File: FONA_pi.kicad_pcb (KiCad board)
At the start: 2 copper layers, 88.4 x 59.1 mm, 35 parts, among them J1 Conn_01x20_Socket, J10 Conn_01x04_Pin, J11 Conn_01x20_Socket, J12 Conn_01x20_Socket, J13 Conn_01x06_Socket, J14 Conn_01x06_Socket, J15 Conn_01x06_Socket, J16 Conn_01x06_Socket, J17 Conn_01x06_Socket, J18 Conn_01x04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

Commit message: Placed footprints again.
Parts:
- removed REF** (x4): MountingHole_2.1mm, MountingHole:MountingHole_2.1mm
- moved JP4 2.58 mm to (144.2, 96.9)
- moved JP3 1.62 mm to (144.2, 93.3)
- moved JP2 0.66 mm to (144.2, 89.8)
- moved J16 0.41 mm to (124.1, 78.4)
- moved JP1 0.27 mm to (144.2, 86.2)
- moved J17 0.18 mm to (124.9, 112.9)

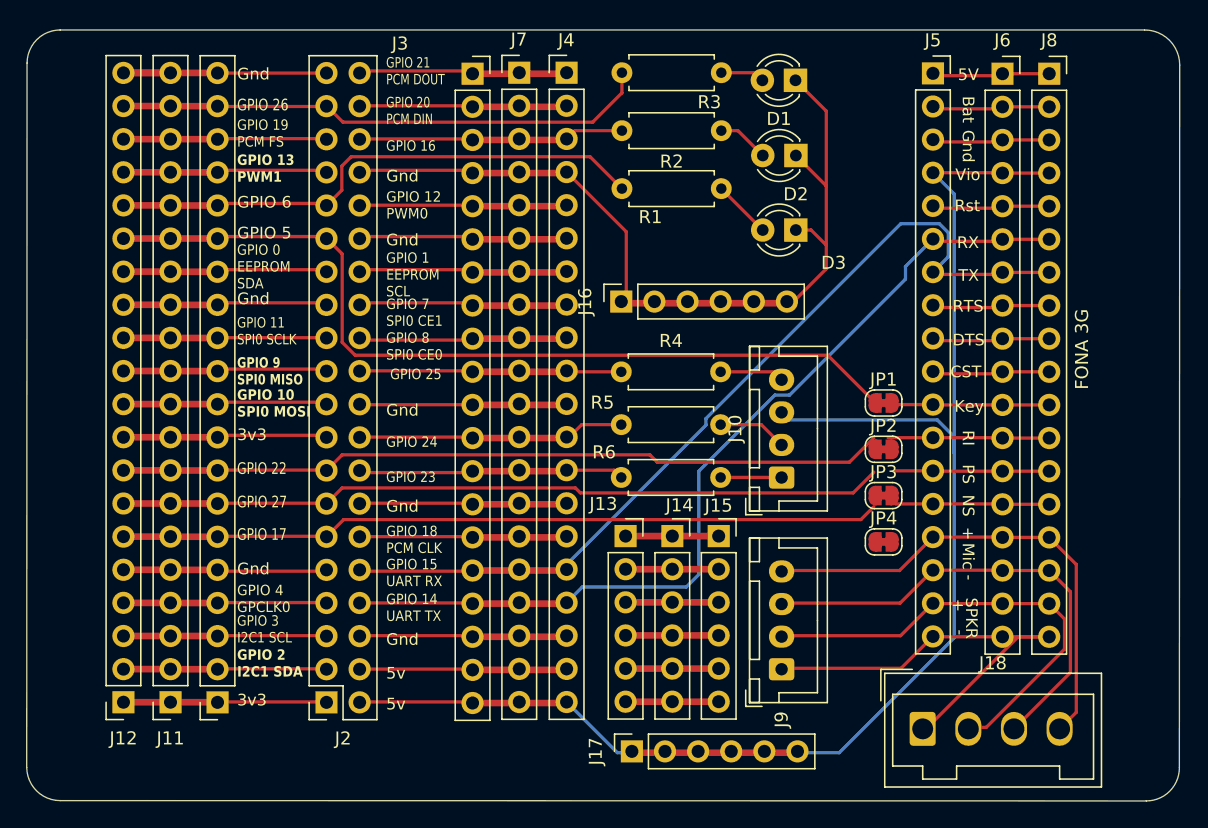
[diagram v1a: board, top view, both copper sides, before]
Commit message: Fixed DRC errors
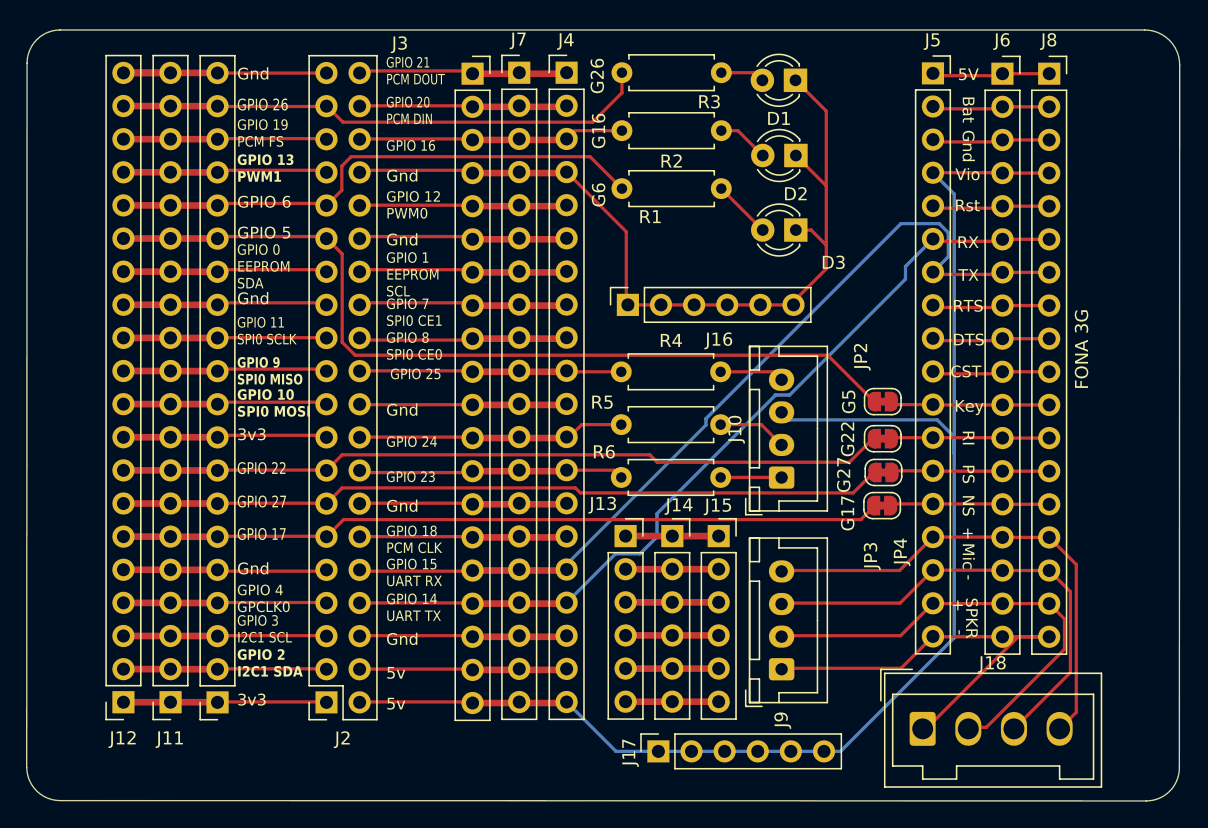
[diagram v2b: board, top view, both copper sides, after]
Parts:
- removed JP1: J2B, Jumper:SolderJumper-2_P1.3mm_Bridged_RoundedPad1.0x1.5mm
- added G5: J2B, Jumper:SolderJumper-2_P1.3mm_Bridged_RoundedPad1.0x1.5mm, F.Cu at (144.1, 86.1)
- moved JP4 2.78 mm to (144.1, 94.1), turned to 180 degrees
- moved J17 2.03 mm to (126.9, 112.9)
- moved JP3 1.77 mm to (144.2, 91.5), turned to 180 degrees
- moved JP2 0.82 mm to (144.1, 89.0), turned to 180 degrees
- moved J16 0.57 mm to (124.6, 78.7)
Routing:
- net Net-(J2-Pin_8): track 68.9 -> 65.4 mm
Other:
- board text added: "G16"
- board text added: "G17"
- board text added: "G22"
- board text added: "G26"
- board text added: "G27"
- board text added: "G6"

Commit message: Labeled some pin connections
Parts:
- moved JP2 0.19 mm to (144.1, 88.8)
- moved JP3 0.13 mm to (144.1, 91.4)
- moved JP4 0.05 mm to (144.1, 94.1)
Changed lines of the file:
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@@
   )
   (footprint "Jumper:SolderJumper-2_P1.3mm_Bridged_RoundedPad1.0x1.5mm" (layer "F.Cu")
-    (at 144.1092 88.9508 180)
+    (at 144.1092 88.764533 180)
     (descr "SMD Solder Jumper, 1x1.5mm, rounded Pads, 0.3mm gap, bridged with 1 copper strip")
     (tags "net tie solder jumper bridged")
@@
     (attr exclude_from_pos_files)
     (net_tie_pad_groups "1, 2")
-    (fp_text reference "G5" (at 2.5804 0 90) (layer "F.SilkS")
+    (fp_text reference "G5" (at 2.7836 0.2032 90) (layer "F.SilkS")
         (effects (font (size 1 1) (thickness 0.15)))
     )
@@
   )
   (footprint "Jumper:SolderJumper-2_P1.3mm_Bridged_RoundedPad1.0x1.5mm" (layer "F.Cu")
-    (at 144.0584 94.0816 180)
+    (at 144.1092 94.0816 180)
     (descr "SMD Solder Jumper, 1x1.5mm, rounded Pads, 0.3mm gap, bridged with 1 copper strip")
     (tags "net tie solder jumper bridged")
@@
   )
   (footprint "Jumper:SolderJumper-2_P1.3mm_Bridged_RoundedPad1.0x1.5mm" (layer "F.Cu")
-    (at 144.16 91.5416 180)
+    (at 144.1092 91.423066 180)
     (descr "SMD Solder Jumper, 1x1.5mm, rounded Pads, 0.3mm gap, bridged with 1 copper strip")
     (tags "net tie solder jumper bridged")
@@
     (effects (font (size 0.8001 0.7112) (thickness 0.0889) bold) (justify left bottom))
   )
+  (gr_text "5v" (at 132.3848 115.6716) (layer "F.SilkS")
+    (effects (font (size 1 1) (thickness 0.15)) (justify left bottom))
+  )
   (gr_text "G16" (at 122.936 66.7512 90) (layer "F.SilkS")
     (effects (font (size 1 1) (thickness 0.15)) (justify left bottom))
@@
     (effects (font (size 0.89408 0.89408) (thickness 0.12192)) (justify bottom))
   )
-  (gr_text "G17" (at 142.0368 96.0628 90) (layer "F.SilkS")
+  (gr_text "G17" (at 142.0876 96.6216 90) (layer "F.SilkS")
     (effects (font (size 1 1) (thickness 0.15)) (justify left bottom))
   )
@@
     (effects (font (size 0.89408 0.89408) (thickness 0.12192)) (justify left))
   )
+  (gr_text "Gnd" (at 122.5296 80.0608 90) (layer "F.SilkS")
+    (effects (font (size 1 1) (thickness 0.15)) (justify left bottom))
+  )
   (gr_text "Vio" (at 149.666476 68.707) (layer "F.SilkS")
     (effects (font (size 0.89408 0.89408) (thickness 0.12192)) (justify left))
@@
     (effects (font (size 0.8001 0.7112) (thickness 0.12192)) (justify left))
   )
-  (gr_text "G27" (at 141.732 93.1164 90) (layer "F.SilkS")
+  (gr_text "G27" (at 141.9352 93.3196 90) (layer "F.SilkS")
     (effects (font (size 1 1) (thickness 0.15)) (justify left bottom))
   )

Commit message: Adjusted text positions
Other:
- board text added: "Rasp Pi Zero"
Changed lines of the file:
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@@
     (attr exclude_from_pos_files)
     (net_tie_pad_groups "1, 2")
-    (fp_text reference "G5" (at 2.7836 0.2032 90) (layer "F.SilkS")
+    (fp_text reference "G5" (at 2.8852 0.4572 90) (layer "F.SilkS")
         (effects (font (size 1 1) (thickness 0.15)))
     )
@@
     (pad "6" thru_hole oval (at 0 12.7 90) (size 1.7 1.7) (drill 1) (layers "*.Cu" "*.Mask")
       (net 63 "Net-(J10-Pin_3)") (pinfunction "Pin_6") (pintype "passive"))
-    (model "${KICAD6_3DMODEL_DIR}/Connector_PinSocket_2.54mm.3dshapes/PinSocket_1x06_P2.54mm_Vertical.wrl"
+    (model "${KICAD6_3DMODEL_DIR}/Connector_PinSocket_2.54mm.3dshapes/PinSocket_1x06_P2.54mm_Vertical.wrl" hide
       (offset (xyz 0 0 0))
       (scale (xyz 1 1 1))
@@
     (pad "6" thru_hole oval (at 0 12.7 90) (size 1.7 1.7) (drill 1) (layers "*.Cu" "*.Mask")
       (net 65 "Net-(D1-K)") (pinfunction "Pin_6") (pintype "passive"))
-    (model "${KICAD6_3DMODEL_DIR}/Connector_PinSocket_2.54mm.3dshapes/PinSocket_1x06_P2.54mm_Vertical.wrl"
+    (model "${KICAD6_3DMODEL_DIR}/Connector_PinSocket_2.54mm.3dshapes/PinSocket_1x06_P2.54mm_Vertical.wrl" hide
       (offset (xyz 0 0 0))
       (scale (xyz 1 1 1))
@@
     (effects (font (size 0.89408 0.89408) (thickness 0.12192)) (justify left))
   )
-  (gr_text "G22" (at 142.0368 90.3732 90) (layer "F.SilkS")
+  (gr_text "G22" (at 141.9115 89.93086 90) (layer "F.SilkS")
     (effects (font (size 1 1) (thickness 0.15)) (justify left bottom))
   )
@@
     (effects (font (size 0.89408 0.89408) (thickness 0.12192)) (justify bottom))
   )
-  (gr_text "G17" (at 142.0876 96.6216 90) (layer "F.SilkS")
+  (gr_text "G17" (at 141.9115 96.3676 90) (layer "F.SilkS")
     (effects (font (size 1 1) (thickness 0.15)) (justify left bottom))
   )
@@
     (effects (font (size 0.89408 0.89408) (thickness 0.12192)) (justify left))
   )
+  (gr_text "Rasp Pi Zero" (at 97.4852 114.0968) (layer "F.SilkS")
+    (effects (font (size 1 1) (thickness 0.15)) (justify left bottom))
+  )
   (gr_text "CST" (at 149.285 83.8246) (layer "F.SilkS")
     (effects (font (size 0.89408 0.89408) (thickness 0.12192)) (justify left))
@@
     (effects (font (size 0.8001 0.7112) (thickness 0.12192)) (justify left))
   )
-  (gr_text "G27" (at 141.9352 93.3196 90) (layer "F.SilkS")
+  (gr_text "G27" (at 141.9115 93.14923 90) (layer "F.SilkS")
     (effects (font (size 1 1) (thickness 0.15)) (justify left bottom))
   )

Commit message: Added mounting holes (again)
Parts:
- added REF**: MountingHole_2.2mm_M2, MountingHole:MountingHole_2.2mm_M2, F.Cu at (81.4, 62.3)
- added REF**: MountingHole_2.2mm_M2, MountingHole:MountingHole_2.2mm_M2, F.Cu at (164.4, 112.3)
- added REF**: MountingHole_2.2mm_M2, MountingHole:MountingHole_2.2mm_M2, F.Cu at (164.4, 62.3)
- added REF**: MountingHole_2.2mm_M2, MountingHole:MountingHole_2.2mm_M2, F.Cu at (81.4, 112.3)
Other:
- board text added: "FONA-Pi Rev 0.1"
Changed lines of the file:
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@@
     )
+  )
+  (footprint "MountingHole:MountingHole_2.2mm_M2" (layer "F.Cu")
+    (at 81.36 62.34)
+    (descr "Mounting Hole 2.2mm, no annular, M2")
+    (tags "mounting hole 2.2mm no annular m2")
+    (attr exclude_from_pos_files exclude_from_bom)
+    (fp_text reference "REF**" (at -0.0508 5.3848) (layer "F.SilkS")
+        (effects (font (size 1 1) (thickness 0.15)))
+    )
+    (fp_text value "MountingHole_2.2mm_M2" (at 0 3.2) (layer "F.Fab")
+        (effects (font (size 1 1) (thickness 0.15)))
+    )
+    (fp_text user "${REFERENCE}" (at 0 0) (layer "F.Fab")
+        (effects (font (size 1 1) (thickness 0.15)))
+    )
+    (fp_circle (center 0 0) (end 2.2 0)
+      (stroke (width 0.15) (type solid)) (fill none) (layer "Cmts.User"))
+    (fp_circle (center 0 0) (end 2.45 0)
+      (stroke (width 0.05) (type solid)) (fill none) (layer "F.CrtYd"))
+    (pad "" np_thru_hole circle (at 0 0) (size 2.2 2.2) (drill 2.2) (layers "*.Cu" "*.Mask"))
   )
   (footprint "Jumper:SolderJumper-2_P1.3mm_Bridged_RoundedPad1.0x1.5mm" (layer "F.Cu")
@@
           (width 0) (fill yes))
       ))
+  )
+  (footprint "MountingHole:MountingHole_2.2mm_M2" (layer "F.Cu")
+    (at 164.36 112.34)
+    (descr "Mounting Hole 2.2mm, no annular, M2")
+    (tags "mounting hole 2.2mm no annular m2")
+    (attr exclude_from_pos_files exclude_from_bom)
+    (fp_text reference "REF**" (at -0.1016 -3.6068) (layer "F.SilkS")
+        (effects (font (size 1 1) (thickness 0.15)))
+    )
+    (fp_text value "MountingHole_2.2mm_M2" (at 0 3.2) (layer "F.Fab")
+        (effects (font (size 1 1) (thickness 0.15)))
+    )
+    (fp_text user "${REFERENCE}" (at 0 0) (layer "F.Fab")
+        (effects (font (size 1 1) (thickness 0.15)))
+    )
+    (fp_circle (center 0 0) (end 2.2 0)
+      (stroke (width 0.15) (type solid)) (fill none) (layer "Cmts.User"))
+    (fp_circle (center 0 0) (end 2.45 0)
+      (stroke (width 0.05) (type solid)) (fill none) (layer "F.CrtYd"))
+    (pad "" np_thru_hole circle (at 0 0) (size 2.2 2.2) (drill 2.2) (layers "F&B.Cu" "*.Mask"))
   )
   (footprint "Connector_PinSocket_2.54mm:PinSocket_1x06_P2.54mm_Vertical" (layer "F.Cu")
@@
     )
   )
+  (footprint "MountingHole:MountingHole_2.2mm_M2" (layer "F.Cu")
+    (at 164.36 62.34)
+    (descr "Mounting Hole 2.2mm, no annular, M2")
+    (tags "mounting hole 2.2mm no annular m2")
+    (attr exclude_from_pos_files exclude_from_bom)
+    (fp_text reference "REF**" (at 0.1016 5.842) (layer "F.SilkS")
+        (effects (font (size 1 1) (thickness 0.15)))
+    )
+    (fp_text value "MountingHole_2.2mm_M2" (at 0 3.2) (layer "F.Fab")
+        (effects (font (size 1 1) (thickness 0.15)))
+    )
+    (fp_text user "${REFERENCE}" (at 0 0) (layer "F.Fab")
+        (effects (font (size 1 1) (thickness 0.15)))
+    )
+    (fp_circle (center 0 0) (end 2.2 0)
+      (stroke (width 0.15) (type solid)) (fill none) (layer "Cmts.User"))
+    (fp_circle (center 0 0) (end 2.45 0)
+      (stroke (width 0.05) (type solid)) (fill none) (layer "F.CrtYd"))
+    (pad "" np_thru_hole circle (at 0 0) (size 2.2 2.2) (drill 2.2) (layers "F&B.Cu" "*.Mask"))
+  )
   (footprint "Connector_PinHeader_2.54mm:PinHeader_1x20_P2.54mm_Vertical" (layer "F.Cu")
     (at 119.8626 60.8838)
@@
     )
   )
+  (footprint "MountingHole:MountingHole_2.2mm_M2" (layer "F.Cu")
+    (at 81.36 112.34)
+    (descr "Mounting Hole 2.2mm, no annular, M2")
+    (tags "mounting hole 2.2mm no annular m2")
+    (attr exclude_from_pos_files exclude_from_bom)
+    (fp_text reference "REF**" (at 0 -3.2) (layer "F.SilkS")
+        (effects (font (size 1 1) (thickness 0.15)))
+    )
+    (fp_text value "MountingHole_2.2mm_M2" (at 0 3.2) (layer "F.Fab")
+        (effects (font (size 1 1) (thickness 0.15)))
+    )
+    (fp_text user "${REFERENCE}" (at 0 0) (layer "F.Fab")
+        (effects (font (size 1 1) (thickness 0.15)))
+    )
+    (fp_circle (center 0 0) (end 2.2 0)
+      (stroke (width 0.15) (type solid)) (fill none) (layer "Cmts.User"))
+    (fp_circle (center 0 0) (end 2.45 0)
+      (stroke (width 0.05) (type solid)) (fill none) (layer "F.CrtYd"))
+    (pad "" np_thru_hole circle (at 0 0) (size 2.2 2.2) (drill 2.2) (layers "F&B.Cu" "*.Mask"))
+  )
   (footprint "Jumper:SolderJumper-2_P1.3mm_Bridged_RoundedPad1.0x1.5mm" (layer "F.Cu")
     (at 144.1092 91.423066 180)
@@
         (effects (font (size 1 1) (thickness 0.15)))
     )
-    (fp_text value "Conn_01x04_Pin" (at 18.6944 4.699 90) (layer "F.Fab")
+    (fp_text value "Conn_01x04_Pin" (at 2.6232 2.54 90) (layer "F.Fab")
         (effects (font (size 1 1) (thickness 0.15)))
     )
@@
         (effects (font (size 1 1) (thickness 0.15)))
     )
-    (fp_text value "Conn_01x06_Socket" (at 0 15.47 90) (layer "F.Fab")
+    (fp_text value "Conn_01x06_Socket" (at 1.9812 5.2324 180) (layer "F.Fab")
         (effects (font (size 1 1) (thickness 0.15)))
     )
@@
   )
   (gr_text "Gnd" (at 122.5296 80.0608 90) (layer "F.SilkS")
+    (effects (font (size 1 1) (thickness 0.15)) (justify left bottom))
+  )
+  (gr_text "FONA-Pi Rev 0.1" (at 143.5608 74.3204 90) (layer "F.SilkS")
     (effects (font (size 1 1) (thickness 0.15)) (justify left bottom))
   )
@@
   (segment (start 103.646699 82.55) (end 139.8882 82.55) (width 0.25) (layer "F.Cu") (net 67))
   (segment (start 101.473 73.6) (end 102.648 74.775) (width 0.25) (layer "F.Cu") (net 67))
+  (group "" (id 28e2c4a3-6a11-4640-9a8d-0be799e9634c)
+    (members
+      5f4713a5-587e-448d-8cbd-0c28c70d9189
+      61c45d73-5b10-46b4-aac7-b92fc013b9e7
+      87b97632-a4bd-424f-b38d-36aae58197f4
+      bb6334c8-253b-4ef1-a0b5-e79c5393b164
+    )
+  )
 )

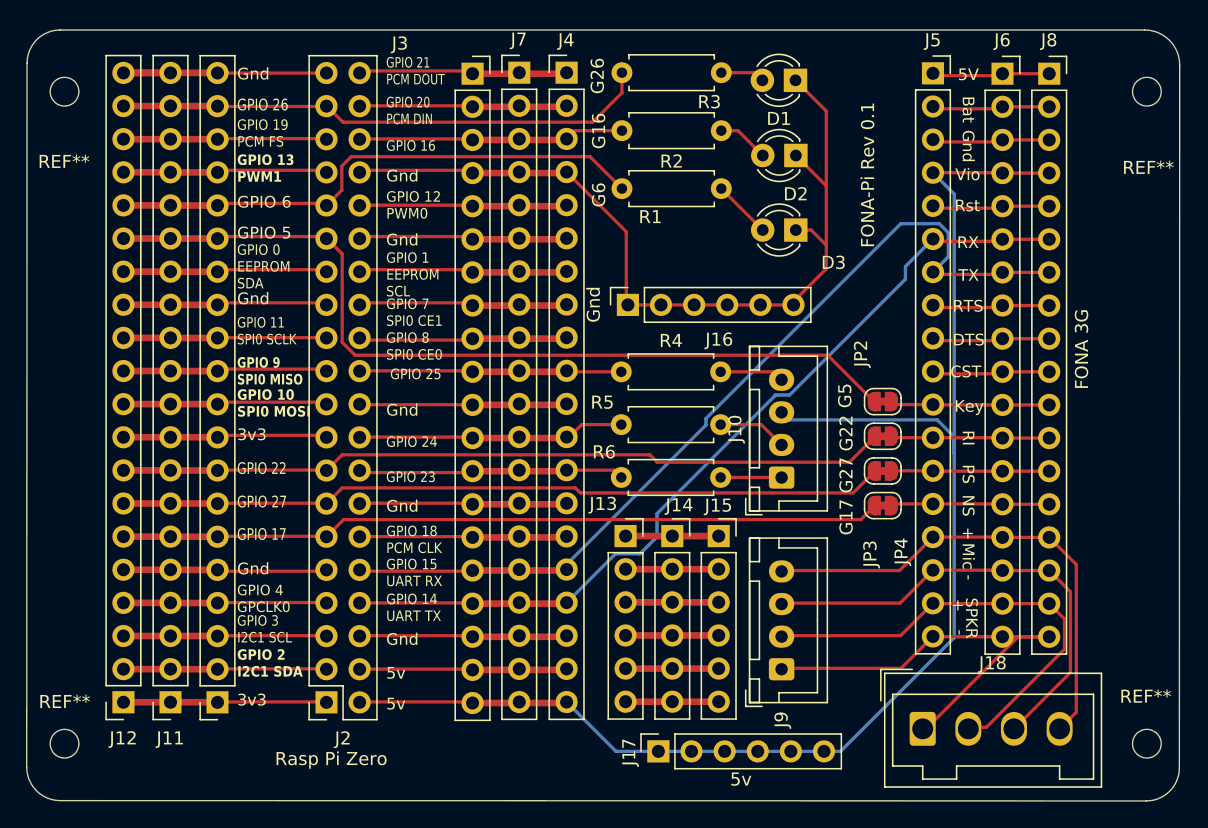
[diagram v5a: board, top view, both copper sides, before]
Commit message: Changed some B.Cu tracks
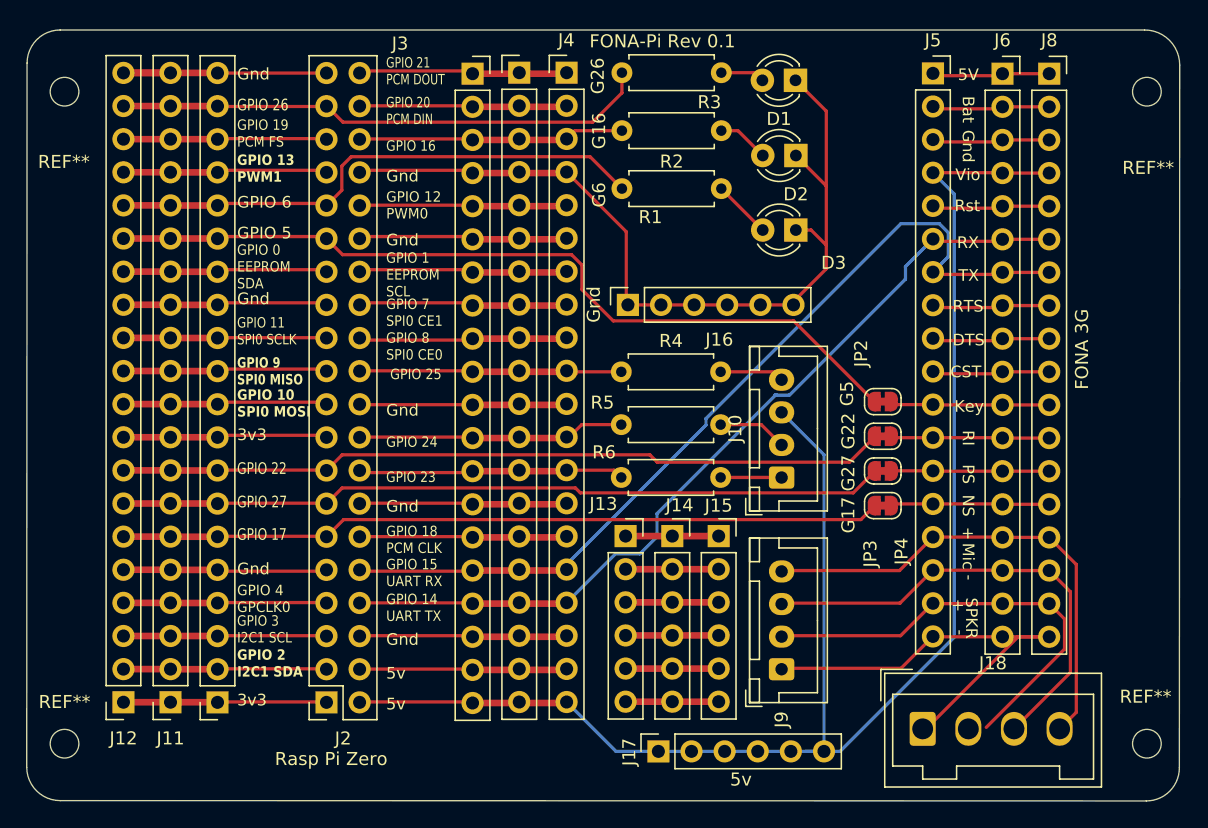
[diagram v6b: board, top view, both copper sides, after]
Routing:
- net Net-(J10-Pin_3): track 111.4 -> 125.6 mm
- net Net-(G5-B): track 66.8 -> 64.1 mm
- net Net-(J18-Pin_2): track 34.4 -> 33.2 mm
